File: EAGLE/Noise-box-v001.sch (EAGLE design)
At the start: 29 parts, among them J1 AVR_SPI_PROG_3X22X3_LOCK, J2 BATT, J4 MICRO-SD_CARD_SOCKET, J5 AUDIO_JACK_3.5MM_SMD, U1 ATMEGA328P_TQFP, U2 MIC5219 3.3V, U3 MCP73831, Y1 12.288MHz

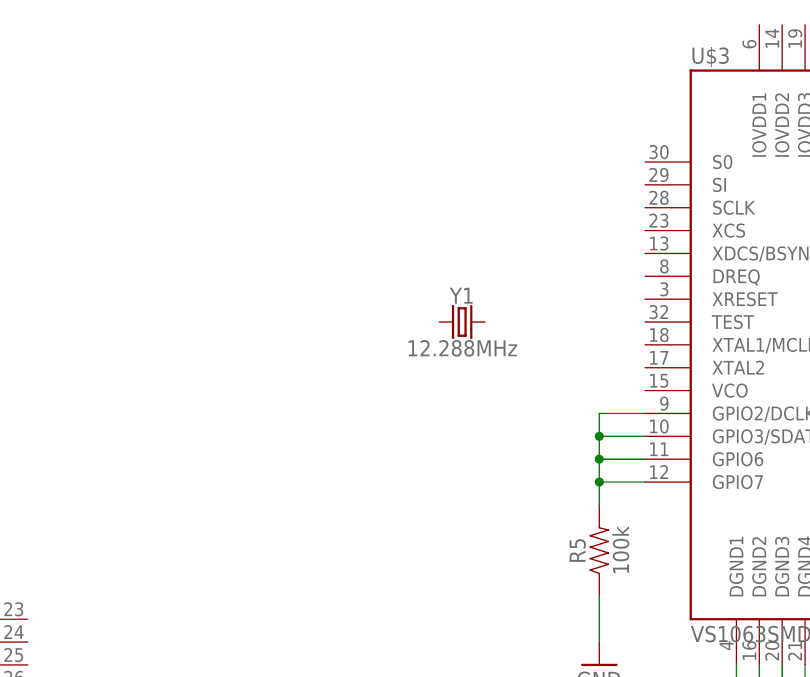
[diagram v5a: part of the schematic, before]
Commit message: clk
Added crystal for vs1063
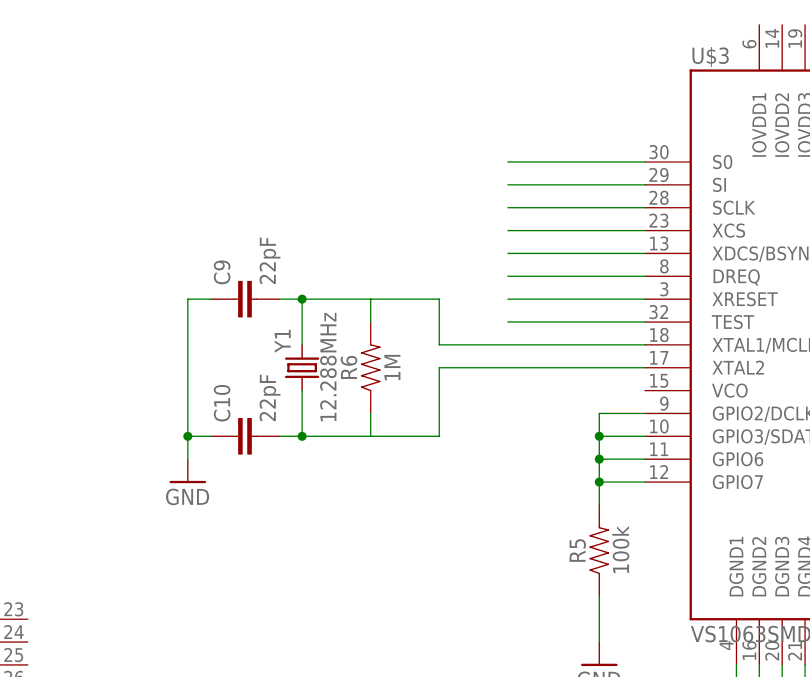
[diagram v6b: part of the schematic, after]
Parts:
- added C10, C9: 22pF, SparkFun-Capacitors:22PF-0603-50V-5%
- added R6: 1M, SparkFun-Resistors:1MOHM-0603-1/4W-5%
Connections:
- new net N$10: U$3.XCS
- new net N$11: U$3.XDCS/BSYNC
- new net N$12: U$3.DREQ
- new net N$13: U$3.XRESET
- new net N$14: U$3.TEST
- new net N$17: C9.2, R6.2, U$3.XTAL1/MCLK, Y1.2
- new net N$18: C10.2, R6.1, U$3.XTAL2, Y1.1
- new net N$7: U$3.S0
- new net N$8: U$3.SI
- new net N$9: U$3.SCLK
- net GND: now also C10.1, C9.1
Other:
- moved on the sheet: Y1
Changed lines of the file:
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@@
 <part name="R5" library="SparkFun-Resistors" deviceset="100KOHM" device="-0603-1/10W-1%" value="100k"/>
 <part name="GND14" library="supply1" deviceset="GND" device=""/>
+<part name="R6" library="SparkFun-Resistors" deviceset="1MOHM" device="-0603-1/4W-5%" value="1M"/>
+<part name="C9" library="SparkFun-Capacitors" deviceset="22PF" device="-0603-50V-5%" value="22pF"/>
+<part name="C10" library="SparkFun-Capacitors" deviceset="22PF" device="-0603-50V-5%" value="22pF"/>
+<part name="GND15" library="supply1" deviceset="GND" device=""/>
 </parts>
 <sheets>
@@
 <instance part="J5" gate="G$1" x="33.02" y="50.8"/>
 <instance part="U$3" gate="G$1" x="347.98" y="226.06"/>
-<instance part="Y1" gate="G$1" x="299.72" y="228.6"/>
+<instance part="Y1" gate="G$1" x="281.94" y="223.52" smashed="yes" rot="R90">
+<attribute name="NAME" x="280.67" y="226.568" size="1.778" layer="95" font="vector" rot="R90" align="bottom-center"/>
+<attribute name="VALUE" x="283.972" y="223.52" size="1.778" layer="96" font="vector" rot="R90" align="top-center"/>
+</instance>
 <instance part="GND13" gate="1" x="347.98" y="180.34"/>
 <instance part="R5" gate="G$1" x="314.96" y="203.2" rot="R90"/>
 <instance part="GND14" gate="1" x="314.96" y="190.5"/>
+<instance part="R6" gate="G$1" x="289.56" y="223.52" rot="R90"/>
+<instance part="C9" gate="G$1" x="276.86" y="231.14" rot="R90"/>
+<instance part="C10" gate="G$1" x="276.86" y="215.9" rot="R90"/>
+<instance part="GND15" gate="1" x="269.24" y="210.82"/>
 </instances>
 <busses>
@@
 <wire x1="314.96" y1="198.12" x2="314.96" y2="193.04" width="0.1524" layer="91"/>
 </segment>
+<segment>
+<pinref part="C9" gate="G$1" pin="1"/>
+<pinref part="GND15" gate="1" pin="GND"/>
+<wire x1="271.78" y1="231.14" x2="269.24" y2="231.14" width="0.1524" layer="91"/>
+<wire x1="269.24" y1="231.14" x2="269.24" y2="215.9" width="0.1524" layer="91"/>
+<pinref part="C10" gate="G$1" pin="1"/>
+<wire x1="269.24" y1="215.9" x2="269.24" y2="213.36" width="0.1524" layer="91"/>
+<wire x1="271.78" y1="215.9" x2="269.24" y2="215.9" width="0.1524" layer="91"/>
+<junction x="269.24" y="215.9"/>
+</segment>
 </net>
 <net name="MOSI" class="0">
@@
 </segment>
 </net>
+<net name="N$7" class="0">
+<segment>
+<pinref part="U$3" gate="G$1" pin="S0"/>
+<wire x1="320.04" y1="246.38" x2="304.8" y2="246.38" width="0.1524" layer="91"/>
+</segment>
+</net>
+<net name="N$8" class="0">
+<segment>
+<pinref part="U$3" gate="G$1" pin="SI"/>
+<wire x1="320.04" y1="243.84" x2="304.8" y2="243.84" width="0.1524" layer="91"/>
+</segment>
+</net>
+<net name="N$9" class="0">
+<segment>
+<pinref part="U$3" gate="G$1" pin="SCLK"/>
+<wire x1="320.04" y1="241.3" x2="304.8" y2="241.3" width="0.1524" layer="91"/>
+</segment>
+</net>
+<net name="N$10" class="0">
+<segment>
+<pinref part="U$3" gate="G$1" pin="XCS"/>
+<wire x1="320.04" y1="238.76" x2="304.8" y2="238.76" width="0.1524" layer="91"/>
+</segment>
+</net>
+<net name="N$11" class="0">
+<segment>
+<pinref part="U$3" gate="G$1" pin="XDCS/BSYNC"/>
+<wire x1="320.04" y1="236.22" x2="304.8" y2="236.22" width="0.1524" layer="91"/>
+</segment>
+</net>
+<net name="N$12" class="0">
+<segment>
+<pinref part="U$3" gate="G$1" pin="DREQ"/>
+<wire x1="320.04" y1="233.68" x2="304.8" y2="233.68" width="0.1524" layer="91"/>
+</segment>
+</net>
+<net name="N$13" class="0">
+<segment>
+<pinref part="U$3" gate="G$1" pin="XRESET"/>
+<wire x1="320.04" y1="231.14" x2="304.8" y2="231.14" width="0.1524" layer="91"/>
+</segment>
+</net>
+<net name="N$14" class="0">
+<segment>
+<pinref part="U$3" gate="G$1" pin="TEST"/>
+<wire x1="320.04" y1="228.6" x2="304.8" y2="228.6" width="0.1524" layer="91"/>
+</segment>
+</net>
+<net name="N$17" class="0">
+<segment>
+<pinref part="U$3" gate="G$1" pin="XTAL1/MCLK"/>
+<wire x1="320.04" y1="226.06" x2="297.18" y2="226.06" width="0.1524" layer="91"/>
+<pinref part="Y1" gate="G$1" pin="2"/>
+<pinref part="C9" gate="G$1" pin="2"/>
+<wire x1="281.94" y1="226.06" x2="281.94" y2="231.14" width="0.1524" layer="91"/>
+<wire x1="281.94" y1="231.14" x2="279.4" y2="231.14" width="0.1524" layer="91"/>
+<pinref part="R6" gate="G$1" pin="2"/>
+<wire x1="289.56" y1="228.6" x2="289.56" y2="231.14" width="0.1524" layer="91"/>
+<wire x1="289.56" y1="231.14" x2="281.94" y2="231.14" width="0.1524" layer="91"/>
+<junction x="281.94" y="231.14"/>
+<wire x1="297.18" y1="226.06" x2="297.18" y2="231.14" width="0.1524" layer="91"/>
+<wire x1="297.18" y1="231.14" x2="289.56" y2="231.14" width="0.1524" layer="91"/>
+</segment>
+</net>
+<net name="N$18" class="0">
+<segment>
+<pinref part="U$3" gate="G$1" pin="XTAL2"/>
+<wire x1="320.04" y1="223.52" x2="297.18" y2="223.52" width="0.1524" layer="91"/>
+<pinref part="C10" gate="G$1" pin="2"/>
+<pinref part="Y1" gate="G$1" pin="1"/>
+<wire x1="279.4" y1="215.9" x2="281.94" y2="215.9" width="0.1524" layer="91"/>
+<wire x1="281.94" y1="215.9" x2="281.94" y2="220.98" width="0.1524" layer="91"/>
+<pinref part="R6" gate="G$1" pin="1"/>
+<wire x1="281.94" y1="215.9" x2="289.56" y2="215.9" width="0.1524" layer="91"/>
+<wire x1="289.56" y1="215.9" x2="289.56" y2="218.44" width="0.1524" layer="91"/>
+<junction x="281.94" y="215.9"/>
+<wire x1="297.18" y1="223.52" x2="297.18" y2="215.9" width="0.1524" layer="91"/>
+<wire x1="297.18" y1="215.9" x2="289.56" y2="215.9" width="0.1524" layer="91"/>
+</segment>
+</net>

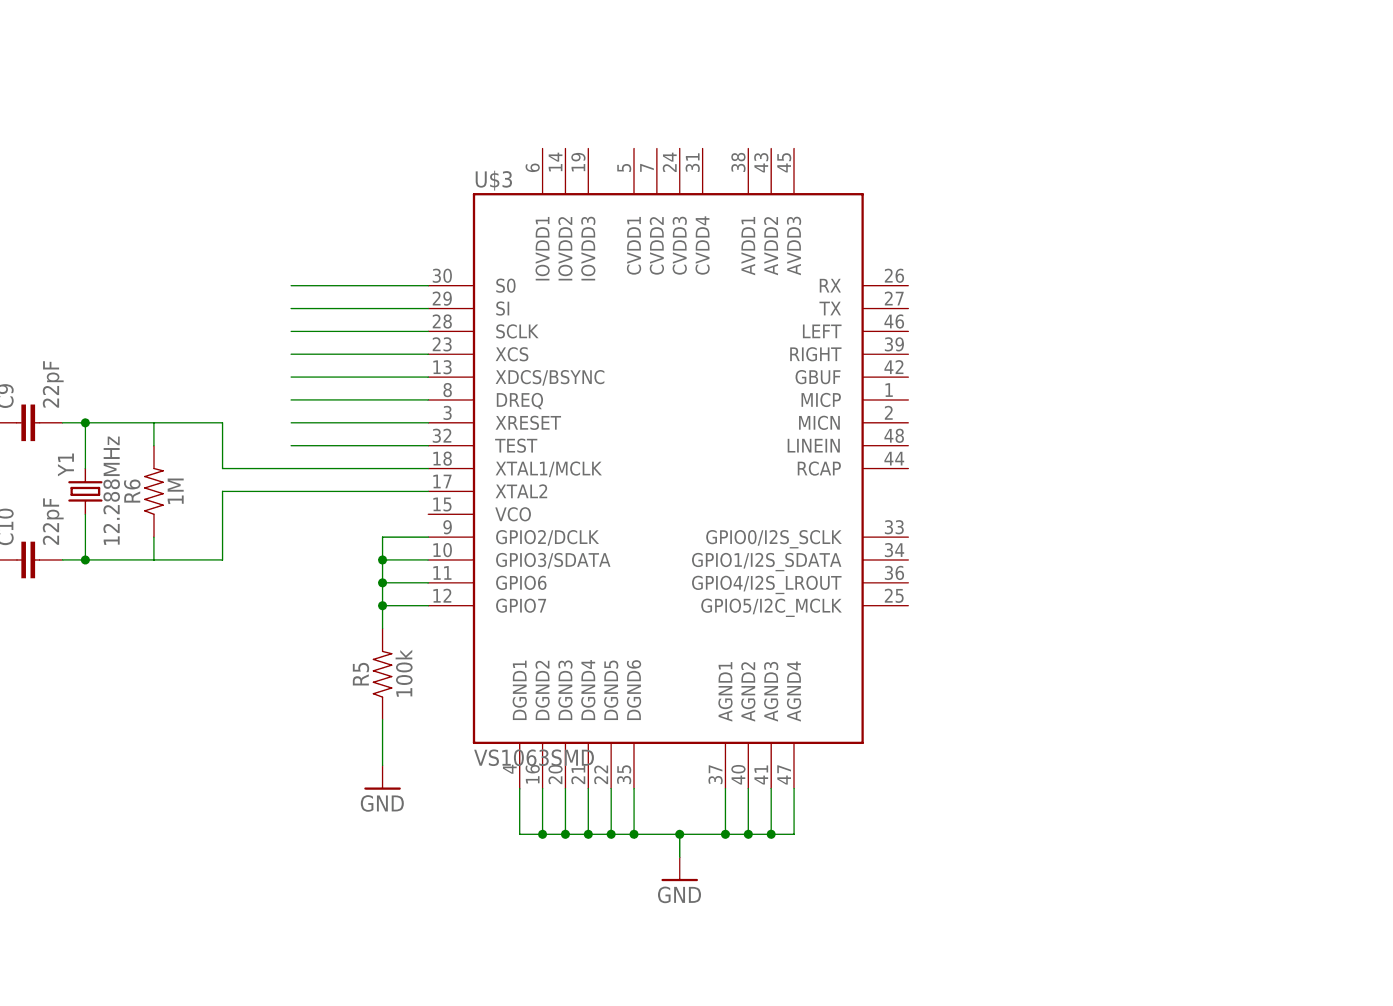
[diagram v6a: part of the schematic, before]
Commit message: vs1063
Added all support circuitry to vs1063, including extra locations for cap
filtering
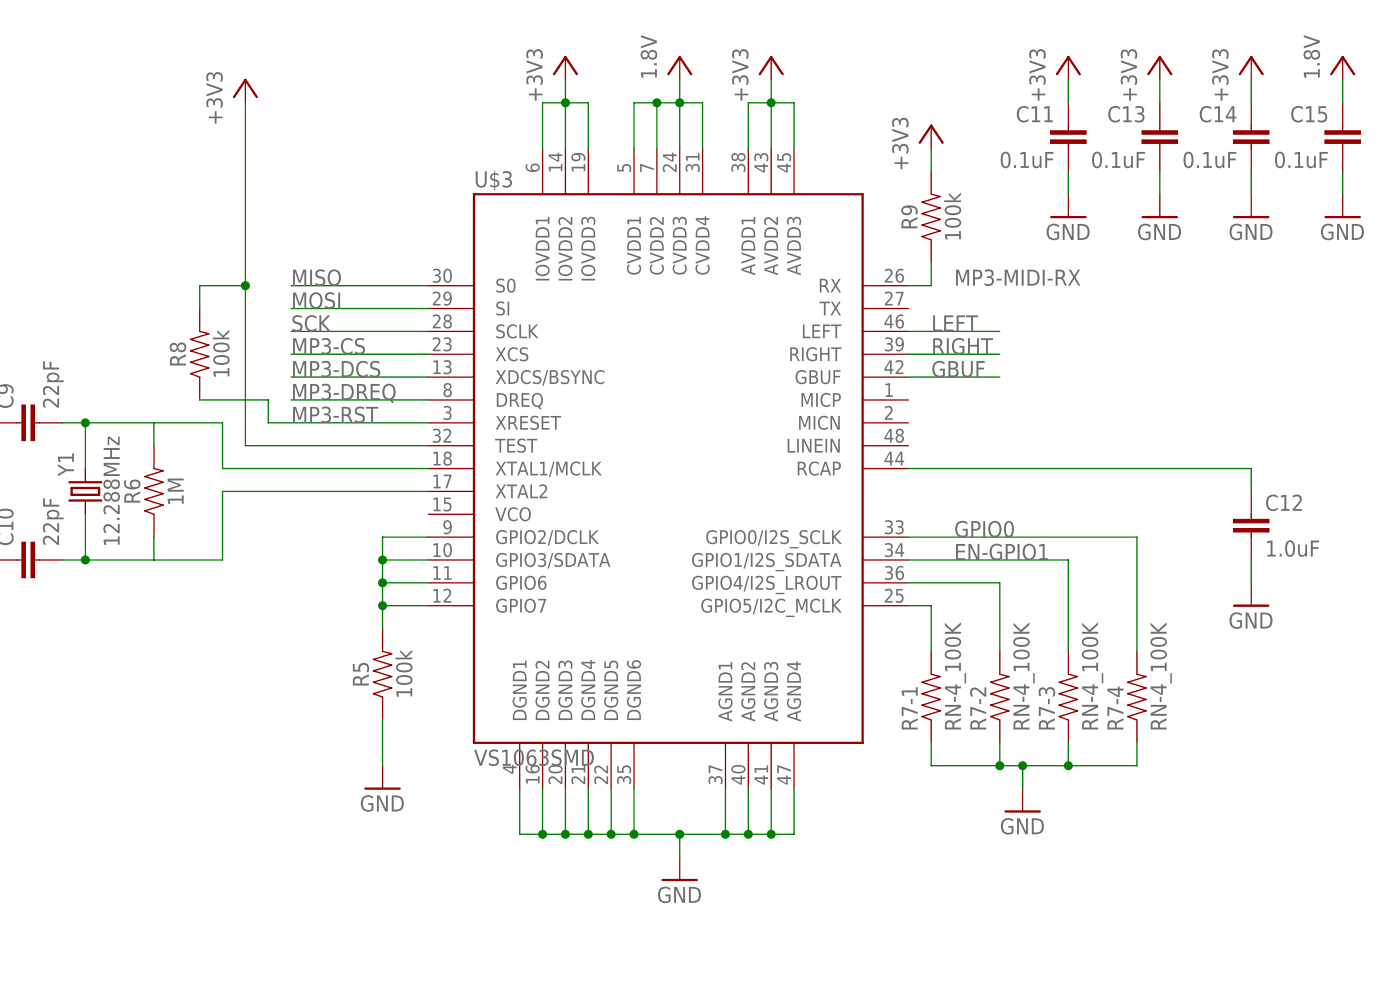
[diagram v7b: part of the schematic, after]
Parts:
- added C11, C13, C14, C15: 0.1uF, SparkFun-Capacitors:0.1UF-0603-25V-5%
- added C12: 1.0uF, SparkFun-Capacitors:1.0UF-0603-16V-10%
- added R7: RN-4_100K, RJC-2:RN-4_100K
- added R8, R9: 100k, SparkFun-Resistors:100KOHM-0603-1/10W-1%
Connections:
- net N$10 renamed MP3-CS
- net N$11 renamed MP3-DCS
- net N$12 renamed MP3-DREQ
- removed net N$13: U$3.XRESET
- removed net N$7: U$3.S0
- removed net N$8: U$3.SI
- removed net N$9: U$3.SCLK
- new net EN-GPIO1: R7-3.2, U$3.GPIO1/I2S_SDATA
- new net GBUF: U$3.GBUF
- new net GPIO0: R7-4.2, U$3.GPIO0/I2S_SCLK
- new net LEFT: U$3.LEFT
- new net MP3-MIDI-RX: R9.1, U$3.RX
- new net MP3-RST: R8.1, U$3.XRESET
- new net N$15: R7-2.2, U$3.GPIO4/I2S_LROUT
- new net N$21: C12.1, U$3.RCAP
- new net RIGHT: U$3.RIGHT
- net +3V3: now also C11.1, C13.1, C14.1, R8.2, R9.2, U$3.AVDD1, U$3.AVDD2, U$3.AVDD3, U$3.IOVDD1, U$3.IOVDD2, U$3.IOVDD3, U$3.TEST
- net GND: now also C11.2, C12.2, C13.2, C14.2, C15.2, R7-1.1, R7-2.1, R7-3.1, R7-4.1
- net MISO: now also U$3.S0
- net MOSI: now also U$3.SI
- net N$14: now also R7-1.2, U$3.GPIO5/I2C_MCLK; no longer U$3.TEST
- net SCK: now also U$3.SCLK
- net VCC: now also C15.1, U$3.CVDD1, U$3.CVDD2, U$3.CVDD3, U$3.CVDD4
